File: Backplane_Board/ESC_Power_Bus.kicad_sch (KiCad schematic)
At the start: 18 parts, among them J21 Conn_01x02_Pin, SW2 SW_DPST_x2, U4 PKJ7213WPI

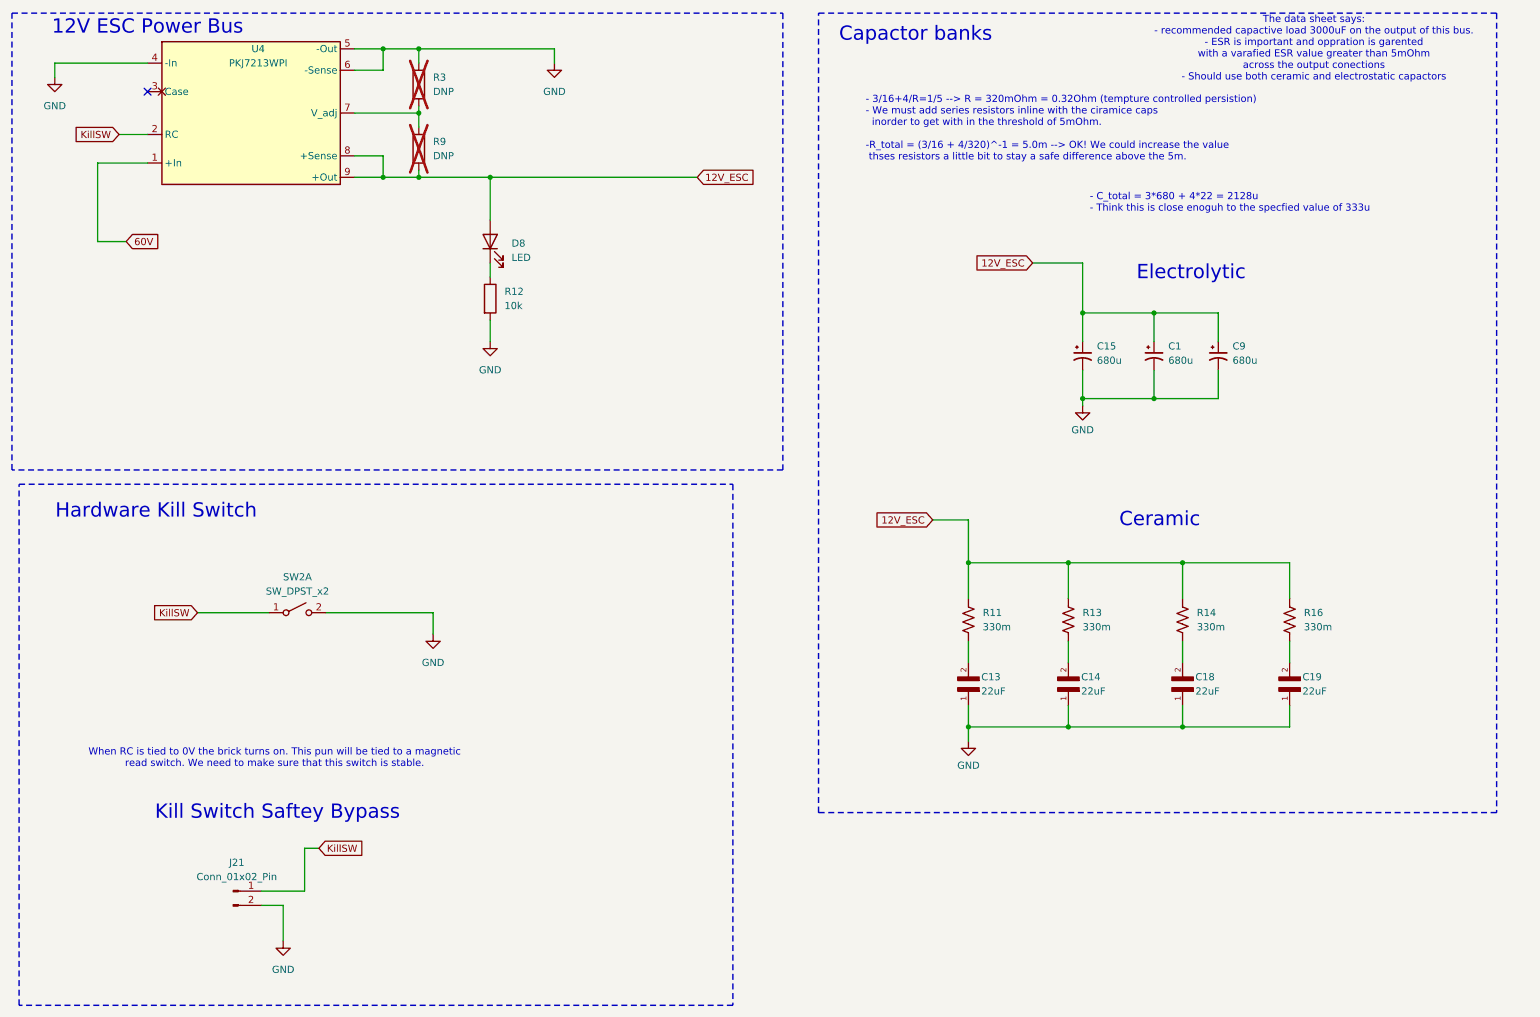
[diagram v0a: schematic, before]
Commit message: update FET circits
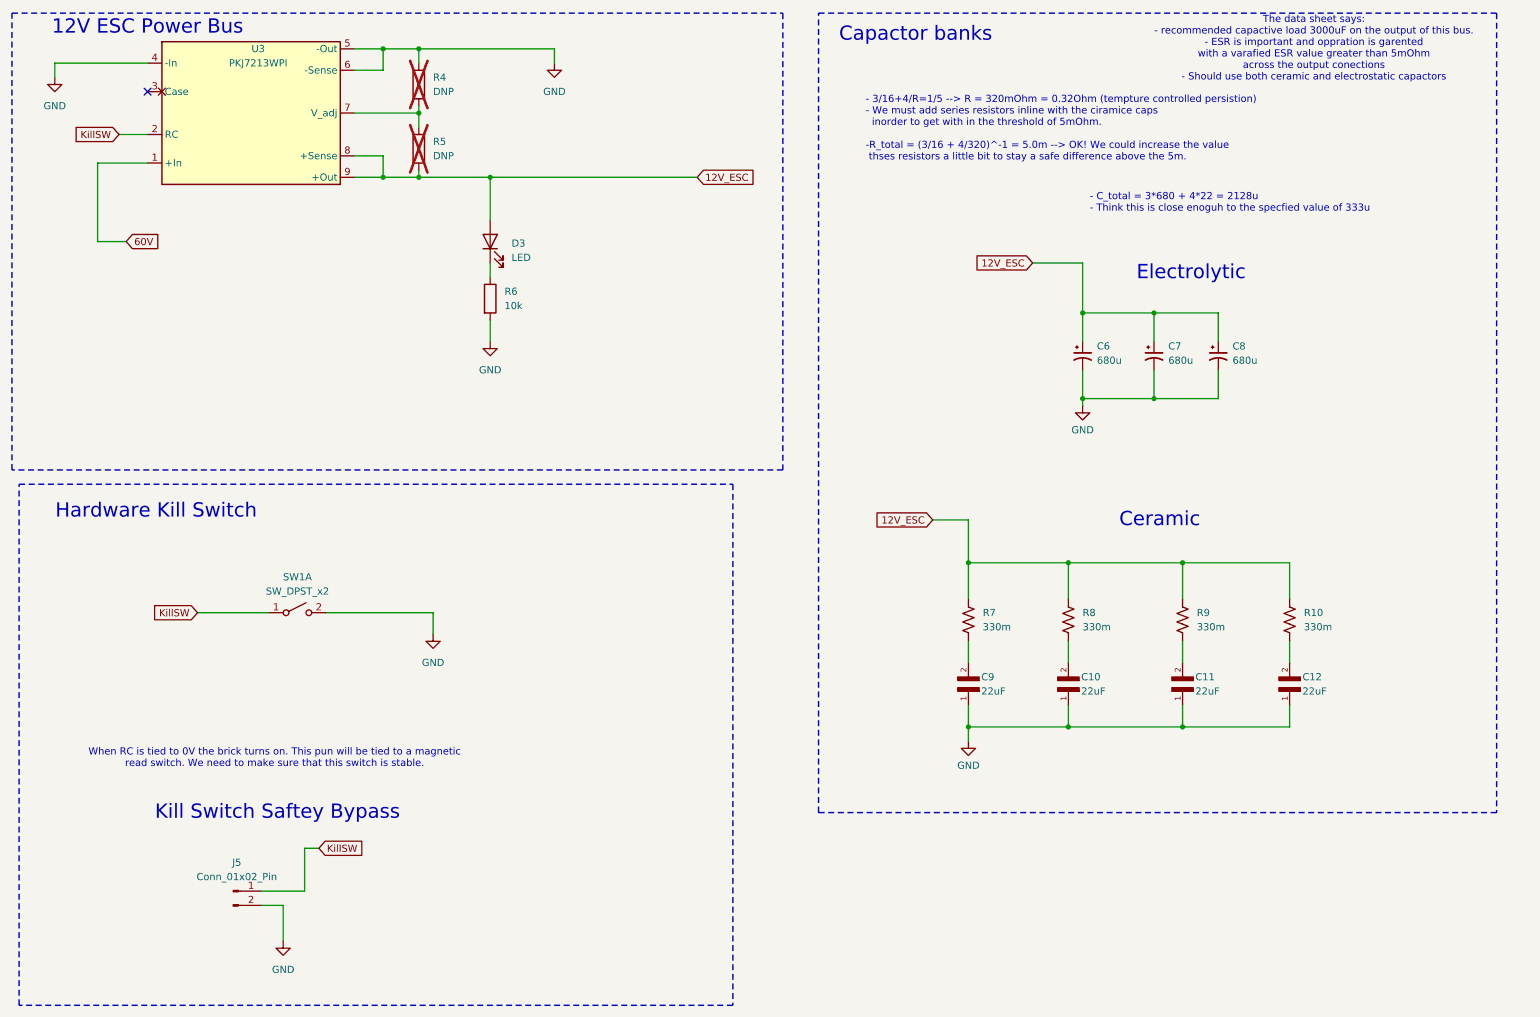
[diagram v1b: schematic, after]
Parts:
- U3: renamed from U4; footprint (none) -> Library:PKJ7213WPI
- renumbered C14 to C10, C18 to C11, C19 to C12, C15 to C6, C1 to C7, C9 to C8, C13 to C9, D8 to D3, J21 to J5, R16 to R10, R3 to R4, R9 to R5, R12 to R6, R11 to R7, R13 to R8, R14 to R9, SW2 to SW1
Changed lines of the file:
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@@
 		(dnp no)
 		(fields_autoplaced yes)
-		(property "Reference" "R13"
+		(property "Reference" "R8"
 			(at 207.01 125.7299 0)
 			(effects
@@
 			(project "Backplane_Board"
 				(path "/4484cfee-9e43-4cef-88b4-a8ca308542b4/f321ebc7-32f1-4bc1-be5e-46cc9e7ab70a"
-					(reference "R13")
+					(reference "R8")
 					(unit 1)
 				)
@@
 		(dnp yes)
 		(fields_autoplaced yes)
-		(property "Reference" "R3"
+		(property "Reference" "R4"
 			(at 91.44 30.4799 0)
 			(effects
@@
 			(project "Backplane_Board"
 				(path "/4484cfee-9e43-4cef-88b4-a8ca308542b4/f321ebc7-32f1-4bc1-be5e-46cc9e7ab70a"
-					(reference "R3")
+					(reference "R4")
 					(unit 1)
 				)
@@
 		(on_board yes)
 		(dnp no)
-		(property "Reference" "C19"
+		(property "Reference" "C12"
 			(at 246.126 137.16 90)
 			(effects
@@
 			(project "Backplane_Board"
 				(path "/4484cfee-9e43-4cef-88b4-a8ca308542b4/f321ebc7-32f1-4bc1-be5e-46cc9e7ab70a"
-					(reference "C19")
+					(reference "C12")
 					(unit 1)
 				)
@@
 		(dnp no)
 		(fields_autoplaced yes)
-		(property "Reference" "R12"
+		(property "Reference" "R6"
 			(at 104.14 68.5799 0)
 			(effects
@@
 			(project "Backplane_Board"
 				(path "/4484cfee-9e43-4cef-88b4-a8ca308542b4/f321ebc7-32f1-4bc1-be5e-46cc9e7ab70a"
-					(reference "R12")
+					(reference "R6")
 					(unit 1)
 				)
@@
 		(dnp no)
 		(fields_autoplaced yes)
-		(property "Reference" "SW2"
+		(property "Reference" "SW1"
 			(at 67.31 119.38 0)
 			(effects
@@
 			(project "Backplane_Board"
 				(path "/4484cfee-9e43-4cef-88b4-a8ca308542b4/f321ebc7-32f1-4bc1-be5e-46cc9e7ab70a"
-					(reference "SW2")
+					(reference "SW1")
 					(unit 1)
 				)
@@
 		(dnp no)
 		(fields_autoplaced yes)
-		(property "Reference" "C9"
+		(property "Reference" "C8"
 			(at 233.68 78.3081 0)
 			(effects
@@
 			(project "Backplane_Board"
 				(path "/4484cfee-9e43-4cef-88b4-a8ca308542b4/f321ebc7-32f1-4bc1-be5e-46cc9e7ab70a"
-					(reference "C9")
+					(reference "C8")
 					(unit 1)
 				)
@@
 		(dnp no)
 		(fields_autoplaced yes)
-		(property "Reference" "R11"
+		(property "Reference" "R7"
 			(at 189.23 125.7299 0)
 			(effects
@@
 			(project ""
 				(path "/4484cfee-9e43-4cef-88b4-a8ca308542b4/f321ebc7-32f1-4bc1-be5e-46cc9e7ab70a"
-					(reference "R11")
+					(reference "R7")
 					(unit 1)
 				)
@@
 		(dnp no)
 		(fields_autoplaced yes)
-		(property "Reference" "#PWR03"
+		(property "Reference" "#PWR022"
 			(at 64.77 190.5 0)
 			(effects
@@
 			(project "Backplane_Board"
 				(path "/4484cfee-9e43-4cef-88b4-a8ca308542b4/f321ebc7-32f1-4bc1-be5e-46cc9e7ab70a"
-					(reference "#PWR03")
+					(reference "#PWR022")
 					(unit 1)
 				)
@@
 		(dnp no)
 		(fields_autoplaced yes)
-		(property "Reference" "D8"
+		(property "Reference" "D3"
 			(at 105.41 60.0074 90)
 			(effects
@@
 			(project "Backplane_Board"
 				(path "/4484cfee-9e43-4cef-88b4-a8ca308542b4/f321ebc7-32f1-4bc1-be5e-46cc9e7ab70a"
-					(reference "D8")
+					(reference "D3")
 					(unit 1)
 				)
@@
 		(on_board yes)
 		(dnp no)
-		(property "Reference" "C14"
+		(property "Reference" "C10"
 			(at 206.756 137.16 90)
 			(effects
@@
 			(project "Backplane_Board"
 				(path "/4484cfee-9e43-4cef-88b4-a8ca308542b4/f321ebc7-32f1-4bc1-be5e-46cc9e7ab70a"
-					(reference "C14")
+					(reference "C10")
 					(unit 1)
 				)
@@
 		(dnp no)
 		(fields_autoplaced yes)
-		(property "Reference" "#PWR021"
+		(property "Reference" "#PWR016"
 			(at 113.03 34.29 0)
 			(effects
@@
 			(project "Backplane_Board"
 				(path "/4484cfee-9e43-4cef-88b4-a8ca308542b4/f321ebc7-32f1-4bc1-be5e-46cc9e7ab70a"
-					(reference "#PWR021")
+					(reference "#PWR016")
 					(unit 1)
 				)
@@
 		(dnp no)
 		(fields_autoplaced yes)
-		(property "Reference" "#PWR011"
+		(property "Reference" "#PWR020"
 			(at 91.44 135.89 0)
 			(effects
@@
 			(project "Backplane_Board"
 				(path "/4484cfee-9e43-4cef-88b4-a8ca308542b4/f321ebc7-32f1-4bc1-be5e-46cc9e7ab70a"
-					(reference "#PWR011")
+					(reference "#PWR020")
 					(unit 1)
 				)
@@
 		(on_board yes)
 		(dnp no)
-		(property "Reference" "C18"
+		(property "Reference" "C11"
 			(at 227.076 137.16 90)
 			(effects
@@
 			(project "Backplane_Board"
 				(path "/4484cfee-9e43-4cef-88b4-a8ca308542b4/f321ebc7-32f1-4bc1-be5e-46cc9e7ab70a"
-					(reference "C18")
+					(reference "C11")
 					(unit 1)
 				)
@@
 		(on_board yes)
 		(dnp no)
-		(property "Reference" "#PWR060"
+		(property "Reference" "#PWR019"
 			(at 207.01 95.25 0)
 			(effects
@@
 			(project "Backplane_Board"
 				(path "/4484cfee-9e43-4cef-88b4-a8ca308542b4/f321ebc7-32f1-4bc1-be5e-46cc9e7ab70a"
-					(reference "#PWR060")
+					(reference "#PWR019")
 					(unit 1)
 				)
@@
 		(dnp no)
 		(fields_autoplaced yes)
-		(property "Reference" "C1"
+		(property "Reference" "C7"
 			(at 222.25 78.3081 0)
 			(effects
@@
 			(project "Backplane_Board"
 				(path "/4484cfee-9e43-4cef-88b4-a8ca308542b4/f321ebc7-32f1-4bc1-be5e-46cc9e7ab70a"
-					(reference "C1")
+					(reference "C7")
 					(unit 1)
 				)
@@
 		(dnp no)
 		(fields_autoplaced yes)
-		(property "Reference" "C15"
+		(property "Reference" "C6"
 			(at 209.55 78.3081 0)
 			(effects
@@
 			(project "Backplane_Board"
 				(path "/4484cfee-9e43-4cef-88b4-a8ca308542b4/f321ebc7-32f1-4bc1-be5e-46cc9e7ab70a"
-					(reference "C15")
+					(reference "C6")
 					(unit 1)
 				)
@@
 		(dnp no)
 		(fields_autoplaced yes)
-		(property "Reference" "R14"
+		(property "Reference" "R9"
 			(at 227.33 125.7299 0)
 			(effects
@@
 			(project "Backplane_Board"
 				(path "/4484cfee-9e43-4cef-88b4-a8ca308542b4/f321ebc7-32f1-4bc1-be5e-46cc9e7ab70a"
-					(reference "R14")
+					(reference "R9")
 					(unit 1)
 				)
@@
 		(dnp no)
 		(fields_autoplaced yes)
-		(property "Reference" "U4"
+		(property "Reference" "U3"
 			(at 60.325 25.4 0)
 			(effects
@@
 			)
 		)
-		(property "Footprint" ""
+		(property "Footprint" "Library:PKJ7213WPI"
 			(at 59.69 36.83 0)
 			(effects
@@
 			(project "Backplane_Board"
 				(path "/4484cfee-9e43-4cef-88b4-a8ca308542b4/f321ebc7-32f1-4bc1-be5e-46cc9e7ab70a"
-					(reference "U4")
+					(reference "U3")
 					(unit 1)
 				)
@@
 		(dnp no)
 		(fields_autoplaced yes)
-		(property "Reference" "#PWR019"
+		(property "Reference" "#PWR017"
 			(at 24.13 36.83 0)
 			(effects
@@
 			(project "Backplane_Board"
 				(path "/4484cfee-9e43-4cef-88b4-a8ca308542b4/f321ebc7-32f1-4bc1-be5e-46cc9e7ab70a"
-					(reference "#PWR019")
+					(reference "#PWR017")
 					(unit 1)
 				)
@@
 		(dnp no)
 		(fields_autoplaced yes)
-		(property "Reference" "J21"
+		(property "Reference" "J5"
 			(at 56.515 170.18 0)
 			(effects
@@
 			(project ""
 				(path "/4484cfee-9e43-4cef-88b4-a8ca308542b4/f321ebc7-32f1-4bc1-be5e-46cc9e7ab70a"
-					(reference "J21")
+					(reference "J5")
 					(unit 1)
 				)
@@
 		(on_board yes)
 		(dnp no)
-		(property "Reference" "C13"
+		(property "Reference" "C9"
 			(at 188.976 137.16 90)
 			(effects
@@
 			(project ""
 				(path "/4484cfee-9e43-4cef-88b4-a8ca308542b4/f321ebc7-32f1-4bc1-be5e-46cc9e7ab70a"
-					(reference "C13")
+					(reference "C9")
 					(unit 1)
 				)
@@
 		(dnp no)
 		(fields_autoplaced yes)
-		(property "Reference" "R16"
+		(property "Reference" "R10"
 			(at 246.38 125.7299 0)
 			(effects
@@
 			(project "Backplane_Board"
 				(path "/4484cfee-9e43-4cef-88b4-a8ca308542b4/f321ebc7-32f1-4bc1-be5e-46cc9e7ab70a"
-					(reference "R16")
+					(reference "R10")
 					(unit 1)
 				)
@@
 		(dnp yes)
 		(fields_autoplaced yes)
-		(property "Reference" "R9"
+		(property "Reference" "R5"
 			(at 91.44 41.9099 0)
 			(effects
@@
 			(project "Backplane_Board"
 				(path "/4484cfee-9e43-4cef-88b4-a8ca308542b4/f321ebc7-32f1-4bc1-be5e-46cc9e7ab70a"
-					(reference "R9")
+					(reference "R5")
 					(unit 1)
 				)
@@
 		(on_board yes)
 		(dnp no)
-		(property "Reference" "#PWR057"
+		(property "Reference" "#PWR021"
 			(at 186.69 154.94 0)
 			(effects
@@
 			(project "Backplane_Board"
 				(path "/4484cfee-9e43-4cef-88b4-a8ca308542b4/f321ebc7-32f1-4bc1-be5e-46cc9e7ab70a"
-					(reference "#PWR057")
+					(reference "#PWR021")
 					(unit 1)
 				)
@@
 		(dnp no)
 		(fields_autoplaced yes)
-		(property "Reference" "#PWR022"
+		(property "Reference" "#PWR018"
 			(at 101.6 83.82 0)
 			(effects
@@
 			(project "Backplane_Board"
 				(path "/4484cfee-9e43-4cef-88b4-a8ca308542b4/f321ebc7-32f1-4bc1-be5e-46cc9e7ab70a"
-					(reference "#PWR022")
-					(unit 1)
-				)
+					(reference "#PWR018")
+					(unit 1)
+				)

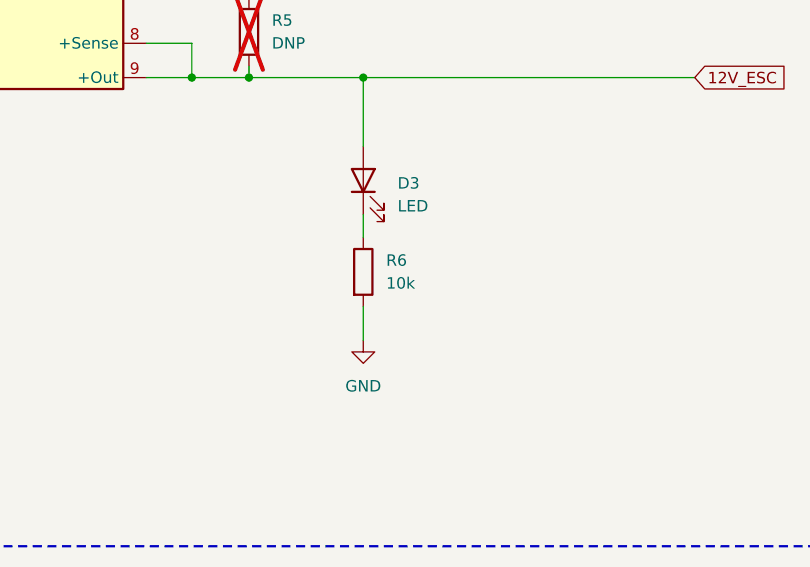
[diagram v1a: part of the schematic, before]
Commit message: adding more footprints
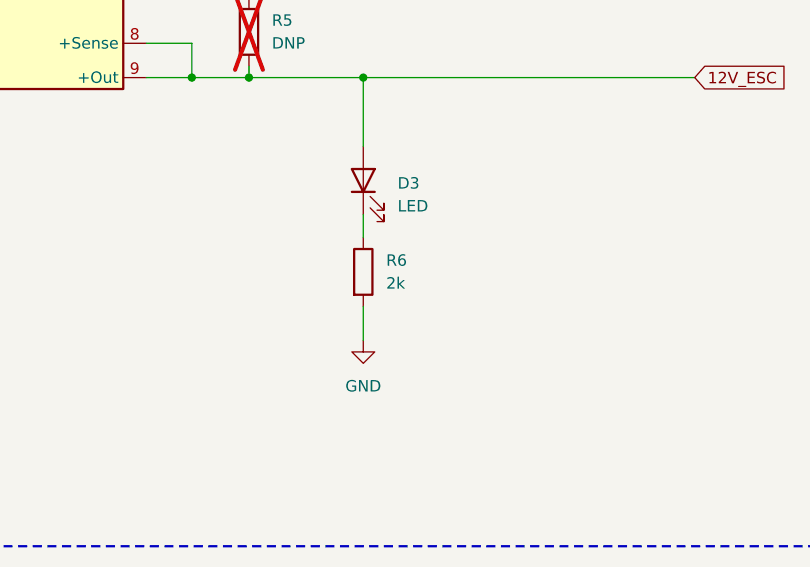
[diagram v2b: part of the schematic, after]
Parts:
- C6, C7, C8: footprint (none) -> Capacitor_THT:CP_Radial_D13.0mm_P5.00mm
- D3: footprint (none) -> LED_SMD:LED_0603_1608Metric
- R4, R5: footprint (none) -> Inductor_SMD:L_1206_3216Metric
- R6: value 10k -> 2k; footprint (none) -> Resistor_SMD:R_1206_3216Metric_Pad1.30x1.75mm_HandSolder
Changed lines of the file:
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@@
 			)
 		)
-		(property "Footprint" ""
+		(property "Footprint" "Inductor_SMD:L_1206_3216Metric"
 			(at 87.122 31.75 90)
 			(effects
@@
 			)
 		)
-		(property "Value" "10k"
+		(property "Value" "2k"
 			(at 104.14 71.1199 0)
 			(effects
@@
 			)
 		)
-		(property "Footprint" ""
+		(property "Footprint" "Resistor_SMD:R_1206_3216Metric_Pad1.30x1.75mm_HandSolder"
 			(at 99.822 69.85 90)
 			(effects
@@
 			)
 		)
-		(property "Footprint" ""
+		(property "Footprint" "Capacitor_THT:CP_Radial_D13.0mm_P5.00mm"
 			(at 231.14 80.01 0)
 			(effects
@@
 			)
 		)
-		(property "Footprint" ""
+		(property "Footprint" "LED_SMD:LED_0603_1608Metric"
 			(at 101.6 59.69 0)
 			(effects
@@
 			)
 		)
-		(property "Footprint" ""
+		(property "Footprint" "Capacitor_THT:CP_Radial_D13.0mm_P5.00mm"
 			(at 219.71 80.01 0)
 			(effects
@@
 			)
 		)
-		(property "Footprint" ""
+		(property "Footprint" "Capacitor_THT:CP_Radial_D13.0mm_P5.00mm"
 			(at 207.01 80.01 0)
 			(effects
@@
 			)
 		)
-		(property "Footprint" ""
+		(property "Footprint" "Inductor_SMD:L_1206_3216Metric"
 			(at 87.122 43.18 90)
 			(effects

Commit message: derat nest ifcation
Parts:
- C10, C11, C12, C9: footprint C2012X5R1V226M125AC:CAPC2012X145N -> Capacitor_SMD:C_1206_3216Metric_Pad1.33x1.80mm_HandSolder
- R6: footprint Resistor_SMD:R_1206_3216Metric_Pad1.30x1.75mm_HandSolder -> Resistor_SMD:R_0805_2012Metric_Pad1.20x1.40mm_HandSolder
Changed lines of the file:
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@@
 			)
 		)
-		(property "Footprint" "C2012X5R1V226M125AC:CAPC2012X145N"
+		(property "Footprint" "Capacitor_SMD:C_1206_3216Metric_Pad1.33x1.80mm_HandSolder"
 			(at 243.84 139.7 0)
 			(effects
@@
 			)
 		)
-		(property "Footprint" "Resistor_SMD:R_1206_3216Metric_Pad1.30x1.75mm_HandSolder"
+		(property "Footprint" "Resistor_SMD:R_0805_2012Metric_Pad1.20x1.40mm_HandSolder"
 			(at 99.822 69.85 90)
 			(effects
@@
 			)
 		)
-		(property "Footprint" "C2012X5R1V226M125AC:CAPC2012X145N"
+		(property "Footprint" "Capacitor_SMD:C_1206_3216Metric_Pad1.33x1.80mm_HandSolder"
 			(at 204.47 139.7 0)
 			(effects
@@
 			)
 		)
-		(property "Footprint" "C2012X5R1V226M125AC:CAPC2012X145N"
+		(property "Footprint" "Capacitor_SMD:C_1206_3216Metric_Pad1.33x1.80mm_HandSolder"
 			(at 224.79 139.7 0)
 			(effects
@@
 			)
 		)
-		(property "Footprint" "C2012X5R1V226M125AC:CAPC2012X145N"
+		(property "Footprint" "Capacitor_SMD:C_1206_3216Metric_Pad1.33x1.80mm_HandSolder"
 			(at 186.69 139.7 0)
 			(effects

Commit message: added gerber
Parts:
- R6: value 2k -> 10k
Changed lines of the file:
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@@
 			)
 		)
-		(property "Value" "2k"
+		(property "Value" "10k"
 			(at 104.14 71.1199 0)
 			(effects
